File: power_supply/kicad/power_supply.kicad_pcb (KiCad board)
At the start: 2 copper layers, 90 x 80 mm, 16 parts, among them J1 pcie_98, J2 Conn_01x05_Socket, U1 URB2405YMD-10WR3, U2 ESD5344D

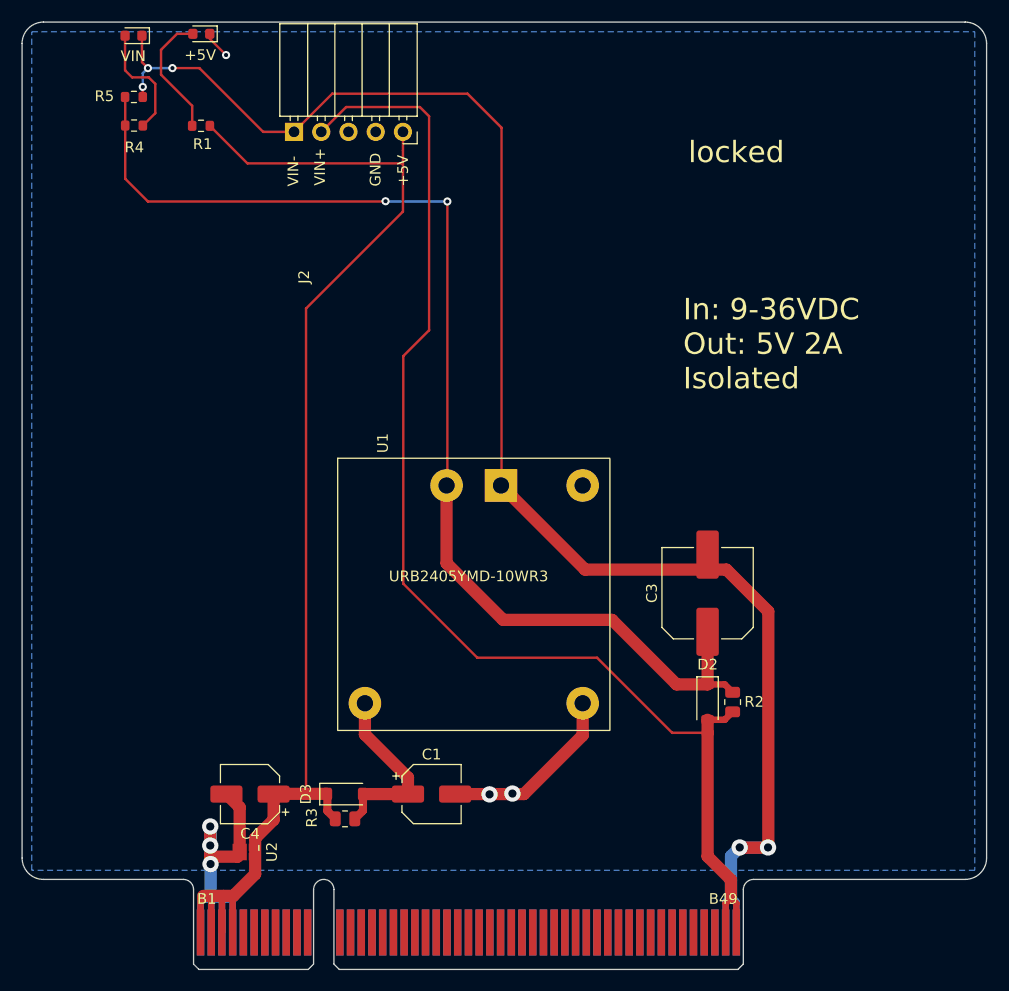
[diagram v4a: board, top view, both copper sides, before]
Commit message: Tweaked the power supply PCB: arranged silkscreen labels, rotated the ESD device.
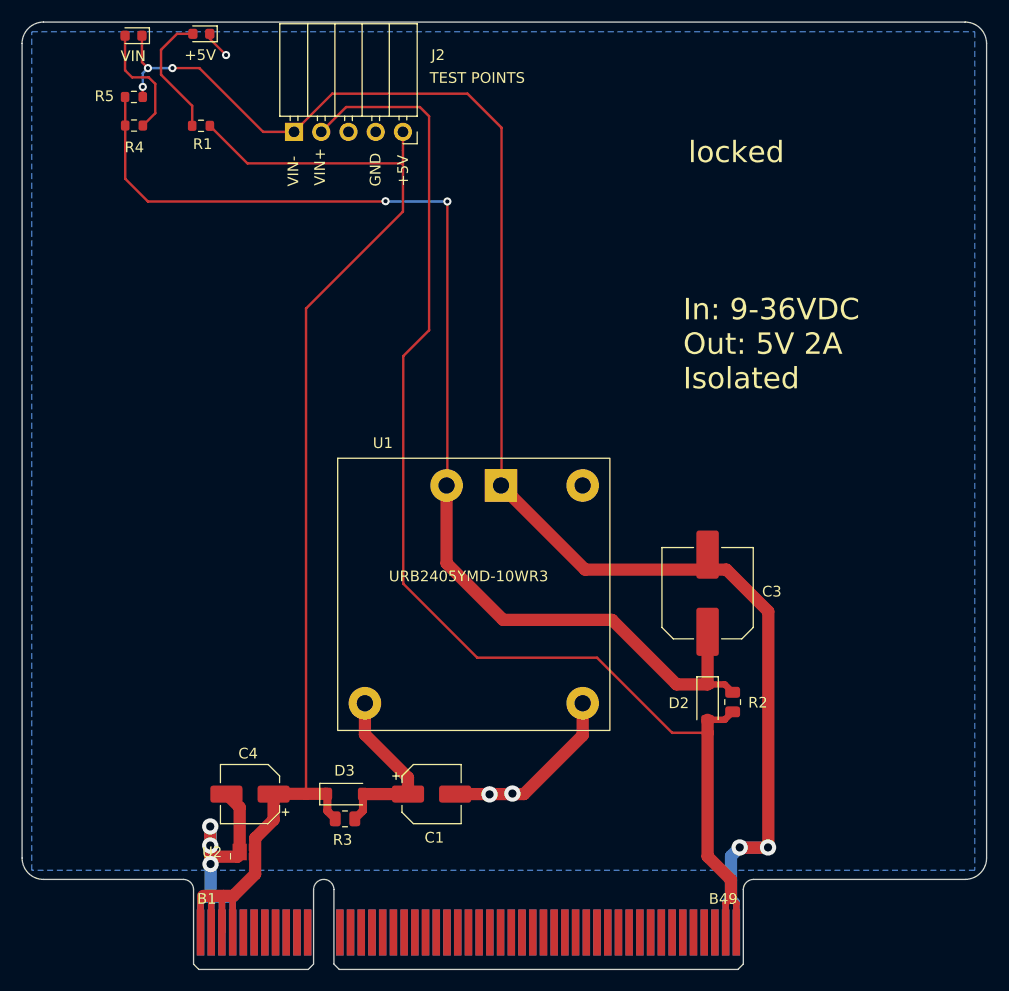
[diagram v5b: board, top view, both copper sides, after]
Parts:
- turned U2 to 90 degrees
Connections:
- U2 pad 1: /+5V -> GND
- U2 pad 2: /+5V -> GND
- U2 pad 4: GND -> /+5V
- U2 pad 5: GND -> /+5V
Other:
- board text added: "TEST POINTS"
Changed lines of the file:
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@@
     (property "ki_keywords" "diode Schottky")
     (attr smd)
-    (fp_text reference "D2" (at -3.5052 0) (layer "F.SilkS")
+    (fp_text reference "D2" (at 0.1016 2.6924) (layer "F.SilkS")
         (effects (font (size 1 1) (thickness 0.15)))
     )
@@
   )
   (footprint "power_supply:Diodes_UDFN-10_1.0x2.5mm_P0.5mm" (layer "F.Cu")
-    (at 62.6204 49.0417 -90)
+    (at 62.6204 49.0417 90)
     (descr "U-DFN2510-10 package used by Diodes Incorporated (https://www.diodes.com/assets/Package-Files/U-DFN2510-10-Type-CJ.pdf)")
     (tags "UDFN-10 U-DFN2510-10 Diodes")
@@
     (property "ki_keywords" "v-to-f v-f")
     (attr smd)
-    (fp_text reference "U2" (at 0 -2.54 90) (layer "F.SilkS")
+    (fp_text reference "U2" (at -0.0197 -3.0386) (layer "F.SilkS")
         (effects (font (size 1 1) (thickness 0.15)))
     )
@@
     (fp_line (start 0.95 1.5) (end -0.95 1.5)
       (stroke (width 0.05) (type solid)) (layer "F.CrtYd"))
-    (pad "1" smd rect (at -0.4375 -1 180) (size 0.25 0.675) (layers "F.Cu" "F.Paste" "F.Mask")
-      (net 14 "/+5V") (pinfunction "D1") (pintype "passive"))
-    (pad "1" smd rect (at 0.4375 -1 180) (size 0.25 0.675) (layers "F.Cu" "F.Paste" "F.Mask")
-      (net 14 "/+5V") (pinfunction "D1") (pintype "passive"))
-    (pad "2" smd rect (at -0.4375 -0.5 180) (size 0.25 0.675) (layers "F.Cu" "F.Paste" "F.Mask")
-      (net 14 "/+5V") (pinfunction "D2") (pintype "passive"))
-    (pad "2" smd rect (at 0.4375 -0.5 180) (size 0.25 0.675) (layers "F.Cu" "F.Paste" "F.Mask")
-      (net 14 "/+5V") (pinfunction "D2") (pintype "passive"))
-    (pad "3" smd rect (at 0 0 180) (size 0.4 1.55) (layers "F.Cu" "F.Paste" "F.Mask")
+    (pad "1" smd rect (at -0.4375 -1) (size 0.25 0.675) (layers "F.Cu" "F.Paste" "F.Mask")
+      (net 1 "GND") (pinfunction "D1") (pintype "passive"))
+    (pad "1" smd rect (at 0.4375 -1) (size 0.25 0.675) (layers "F.Cu" "F.Paste" "F.Mask")
+      (net 1 "GND") (pinfunction "D1") (pintype "passive"))
+    (pad "2" smd rect (at -0.4375 -0.5) (size 0.25 0.675) (layers "F.Cu" "F.Paste" "F.Mask")
+      (net 1 "GND") (pinfunction "D2") (pintype "passive"))
+    (pad "2" smd rect (at 0.4375 -0.5) (size 0.25 0.675) (layers "F.Cu" "F.Paste" "F.Mask")
+      (net 1 "GND") (pinfunction "D2") (pintype "passive"))
+    (pad "3" smd rect (at 0 0) (size 0.4 1.55) (layers "F.Cu" "F.Paste" "F.Mask")
       (net 1 "GND") (pinfunction "GND") (pintype "power_in"))
-    (pad "4" smd rect (at -0.4375 0.5 180) (size 0.25 0.675) (layers "F.Cu" "F.Paste" "F.Mask")
-      (net 1 "GND") (pinfunction "D3") (pintype "passive"))
-    (pad "4" smd rect (at 0.4375 0.5 180) (size 0.25 0.675) (layers "F.Cu" "F.Paste" "F.Mask")
-      (net 1 "GND") (pinfunction "D3") (pintype "passive"))
-    (pad "5" smd rect (at -0.4375 1 180) (size 0.25 0.675) (layers "F.Cu" "F.Paste" "F.Mask")
-      (net 1 "GND") (pinfunction "D4") (pintype "passive"))
-    (pad "5" smd rect (at 0.4375 1 180) (size 0.25 0.675) (layers "F.Cu" "F.Paste" "F.Mask")
-      (net 1 "GND") (pinfunction "D4") (pintype "passive"))
+    (pad "4" smd rect (at -0.4375 0.5) (size 0.25 0.675) (layers "F.Cu" "F.Paste" "F.Mask")
+      (net 14 "/+5V") (pinfunction "D3") (pintype "passive"))
+    (pad "4" smd rect (at 0.4375 0.5) (size 0.25 0.675) (layers "F.Cu" "F.Paste" "F.Mask")
+      (net 14 "/+5V") (pinfunction "D3") (pintype "passive"))
+    (pad "5" smd rect (at -0.4375 1) (size 0.25 0.675) (layers "F.Cu" "F.Paste" "F.Mask")
+      (net 14 "/+5V") (pinfunction "D4") (pintype "passive"))
+    (pad "5" smd rect (at 0.4375 1) (size 0.25 0.675) (layers "F.Cu" "F.Paste" "F.Mask")
+      (net 14 "/+5V") (pinfunction "D4") (pintype "passive"))
     (model "${KIPRJMOD}/3d_models/esd_diode_x4.step"
       (offset (xyz 0 0 0))
@@
     (property "ki_keywords" "connector")
     (attr through_hole)
-    (fp_text reference "J2" (at -4.146 13.5328 90) (layer "F.SilkS")
+    (fp_text reference "J2" (at 8.362 -7.1686 180) (layer "F.SilkS")
         (effects (font (size 1 1) (thickness 0.15)))
     )
@@
     (property "ki_keywords" "cap capacitor")
     (attr smd)
-    (fp_text reference "C3" (at 0 -5.2 90) (layer "F.SilkS")
+    (fp_text reference "C3" (at 0.1524 5.9944 180) (layer "F.SilkS")
         (effects (font (size 1 1) (thickness 0.15)))
     )
@@
     (property "ki_keywords" "R res resistor")
     (attr smd)
-    (fp_text reference "R3" (at 3.0997 0.1016 90) (layer "F.SilkS")
+    (fp_text reference "R3" (at 0.2286 -1.9558 180) (layer "F.SilkS")
         (effects (font (size 1 1) (thickness 0.15)))
     )
@@
     (property "ki_keywords" "cap capacitor")
     (attr smd)
-    (fp_text reference "C1" (at 0 -3.7) (layer "F.SilkS")
+    (fp_text reference "C1" (at 0.254 4.064) (layer "F.SilkS")
         (effects (font (size 1 1) (thickness 0.15)))
     )
@@
     (property "ki_keywords" "diode Schottky")
     (attr smd exclude_from_bom)
-    (fp_text reference "D3" (at -3.6566 0 90) (layer "F.SilkS")
+    (fp_text reference "D3" (at -0.0508 -2.1844 180) (layer "F.SilkS")
         (effects (font (size 1 1) (thickness 0.15)))
     )
@@
     (property "ki_keywords" "DC/DC converter dual")
     (attr through_hole)
-    (fp_text reference "U1" (at -8.4862 -14.1174 90) (layer "F.SilkS")
+    (fp_text reference "U1" (at -8.4862 -14.1174 180) (layer "F.SilkS")
         (effects (font (size 1 1) (thickness 0.15)))
     )
@@
     (property "ki_keywords" "cap capacitor")
     (attr smd)
-    (fp_text reference "C4" (at 0 -3.7) (layer "F.SilkS")
+    (fp_text reference "C4" (at 0.1778 3.7846) (layer "F.SilkS")
         (effects (font (size 1 1) (thickness 0.15)))
     )
@@
     (property "ki_keywords" "R res resistor")
     (attr smd exclude_from_bom)
-    (fp_text reference "R2" (at 0.0254 2.0066 180) (layer "F.SilkS")
+    (fp_text reference "R2" (at -0.0508 2.3622 180) (layer "F.SilkS")
         (effects (font (size 1 1) (thickness 0.15)))
     )
@@
     (effects (font (size 2 2) (thickness 0.2)) (justify left bottom))
   )
+  (gr_text "TEST POINTS" (at 79.883 -23.1902) (layer "F.SilkS")
+    (effects (font (size 1 1) (thickness 0.15)) (justify left))
+  )
   (gr_text "+5V" (at 77.3938 -13.0556 90) (layer "F.SilkS")

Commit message: Simplified the power supply. Removed jumper resistors and output diode. Replaced reverse current leakage resistor with a diode.
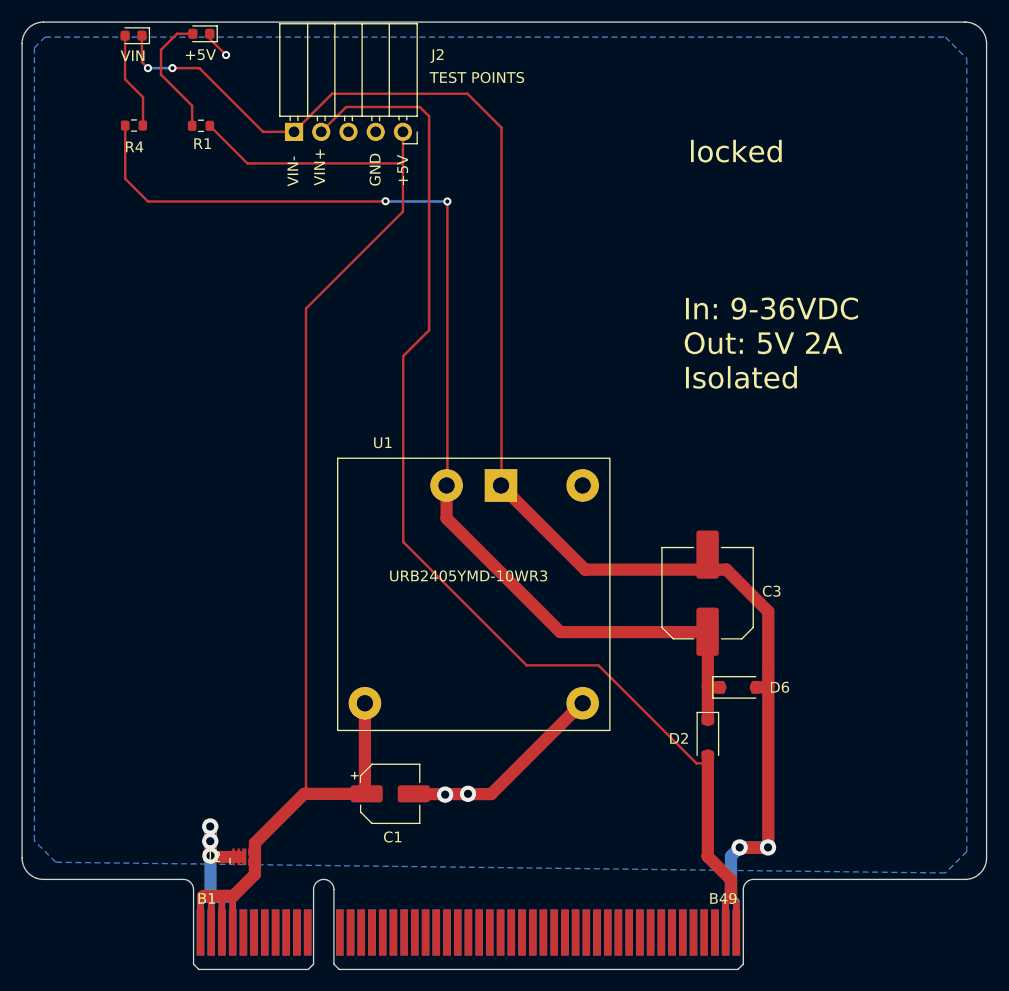
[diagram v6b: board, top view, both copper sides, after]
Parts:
- removed C4: 100uf 10V, Capacitor_SMD:CP_Elec_5x5.4
- removed D3: B5819W SL, Diode_SMD:D_SOD-123
- removed R2, R3: 0R, Resistor_SMD:R_0805_2012Metric
- removed R5: 100K, Resistor_SMD:R_0603_1608Metric
- added D6: B5819W SL, Diode_SMD:D_SOD-123, F.Cu at (108.7, 33.7)
- R4: value 20K -> 15K
- moved C1 3.86 mm to (76.2, 43.6)
- moved D2 3.33 mm to (105.8, 38.4)
- moved U2 0.45 mm to (62.6, 49.5)
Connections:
- C1 pad 1: Net-(D3-A) -> /+5V
- U1 pad 3: Net-(D3-A) -> /+5V
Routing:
- net Net-(D3-A): track 16.7 -> 0.00 mm
- net /+5V: track 120.3 -> 128.3 mm
- net /VIN+: track 117.2 -> 110.4 mm
- net GND: track 56.9 -> 51.3 mm
- net Net-(D2-K): track 109.0 -> 103.7 mm
- net Net-(D1-A): track 10.9 -> 9.08 mm
- net /VIN-: track 147.0 -> 145.4 mm, vias 5 -> 4

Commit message: More power supply pcb cleanup
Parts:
- added F1: 1.25A, Fuse:Fuse_1206_3216Metric, F.Cu at (105.9, 44.9)
- added F2: 1.25A, Fuse:Fuse_1206_3216Metric, F.Cu at (111.4, 44.9)
- added F3: 2A, Fuse:Fuse_1206_3216Metric, F.Cu at (68.9, 43.6)
- added R2: 1K, Resistor_SMD:R_0603_1608Metric, F.Cu at (67.2, -10.6)
- added R3: 1K, Resistor_SMD:R_0603_1608Metric, F.Cu at (69.8, -10.6)
- added R5: 1K, Resistor_SMD:R_0603_1608Metric, F.Cu at (74.9, -10.6)
- added R6: 1K, Resistor_SMD:R_0603_1608Metric, F.Cu at (77.4, -10.7)
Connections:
- C1 pad 1: /+5V -> Net-(U1-+VOUT)
- C3 pad 2: /VIN- -> Net-(D1-K)
- D1 pad 1: /VIN- -> Net-(D1-K)
- D2 pad 2: /VIN+ -> Net-(D2-A)
- D6 pad 2: /VIN- -> Net-(D1-K)
- J2 pad 1: /VIN- -> Net-(J2-Pin_1)
- J2 pad 2: /VIN+ -> Net-(J2-Pin_2)
- J2 pad 4: GND -> Net-(J2-Pin_4)
- J2 pad 5: /+5V -> Net-(J2-Pin_5)
- U1 pad 1: /VIN- -> Net-(D1-K)
- U1 pad 3: /+5V -> Net-(U1-+VOUT)
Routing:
- net Net-(D1-K): track 0.00 -> 118.2 mm, vias 0 -> 2
- net /VIN+: track 110.4 -> 91.3 mm
- net /+5V: track 128.3 -> 110.2 mm, vias 0 -> 2
- net Net-(U1-+VOUT): track 0.00 -> 12.2 mm
- net /VIN-: track 145.4 -> 134.0 mm
- net Net-(D2-K): track 103.7 -> 94.0 mm
- net Net-(J2-Pin_2): track 0.00 -> 6.72 mm
- net Net-(J2-Pin_1): track 0.00 -> 6.72 mm
- net Net-(J2-Pin_4): track 0.00 -> 6.70 mm
- net Net-(J2-Pin_5): track 0.00 -> 6.63 mm
- net Net-(D2-A): track 0.00 -> 3.47 mm
- net GND: track 51.3 -> 52.6 mm, vias 6 -> 7

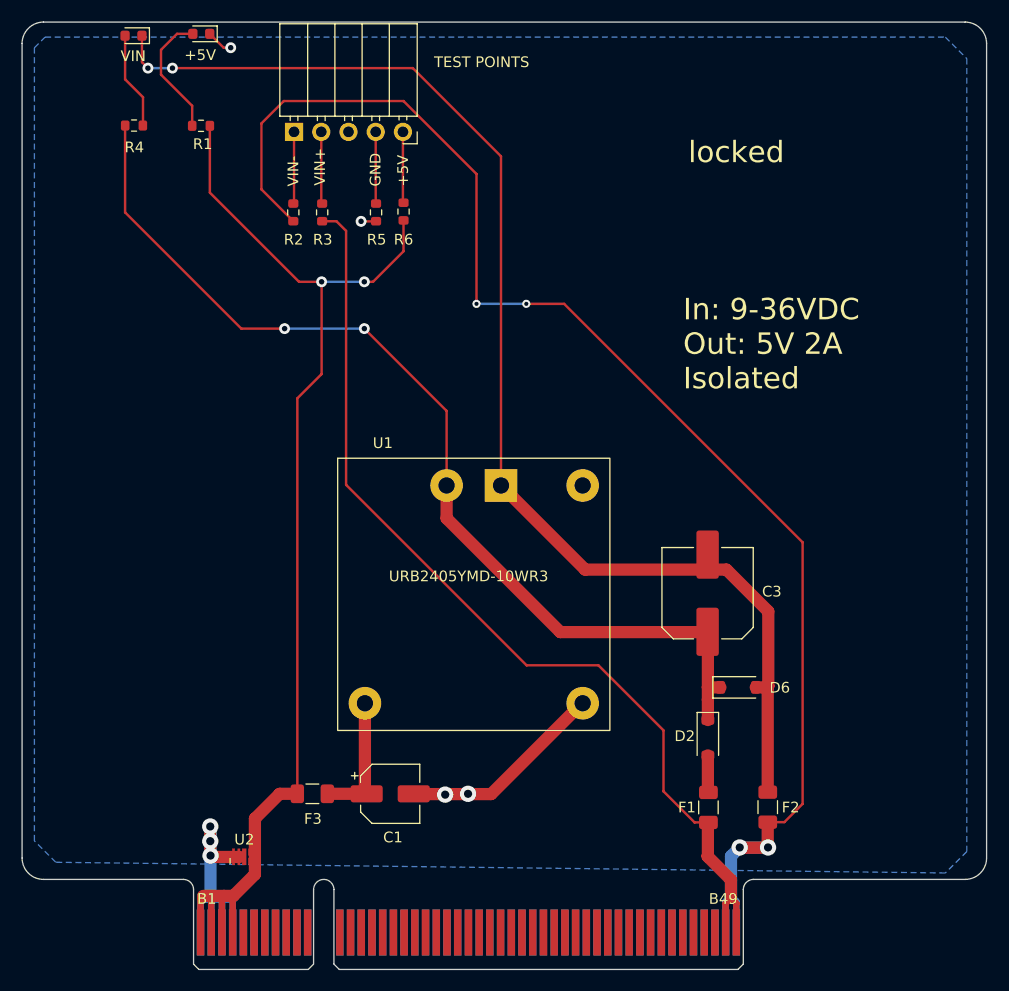
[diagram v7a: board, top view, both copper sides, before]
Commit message: Changed the power supply board to use common symbol and footprints from 'common'.
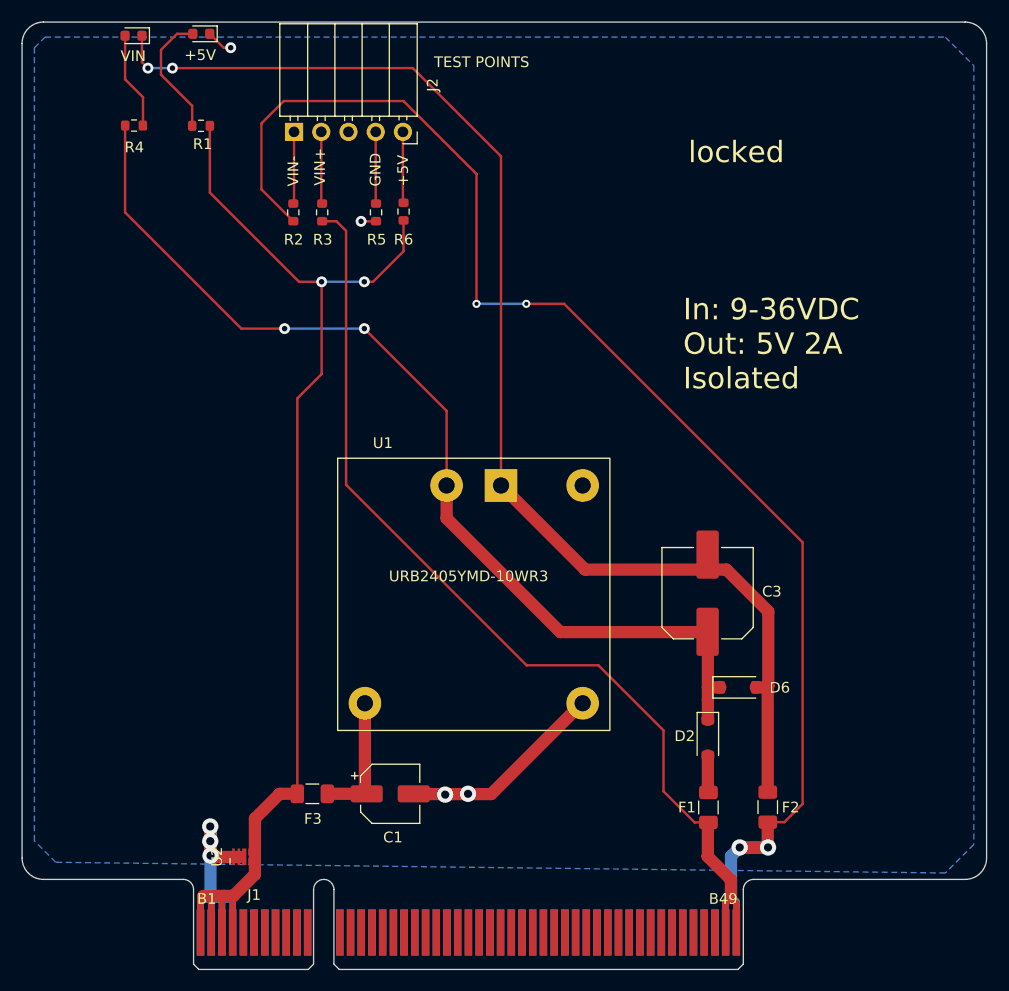
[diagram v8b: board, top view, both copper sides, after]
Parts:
- J1: footprint power_supply:pcie_98_edge -> common:PCIE_98_CARD
- J2: footprint power_supply:PinSocket_1x05_P2.54mm_Horizontal -> common:PinSocket_1x05_P2.54mm_Horizontal_JLCPCB
- U2: footprint power_supply:Diodes_UDFN-10_1.0x2.5mm_P0.5mm -> common:Diodes_UDFN-10_1.0x2.5mm_P0.5mm
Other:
- board size 90 x 80 mm -> 90 x 88.4 mm
